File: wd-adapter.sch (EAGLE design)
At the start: 34 parts, among them Q1 BS170, Q2 BS170, Q3 BS170, Q4 BS170, Q5 BS170, Q6 BS170, T1 BC337, X2 KUSBVX

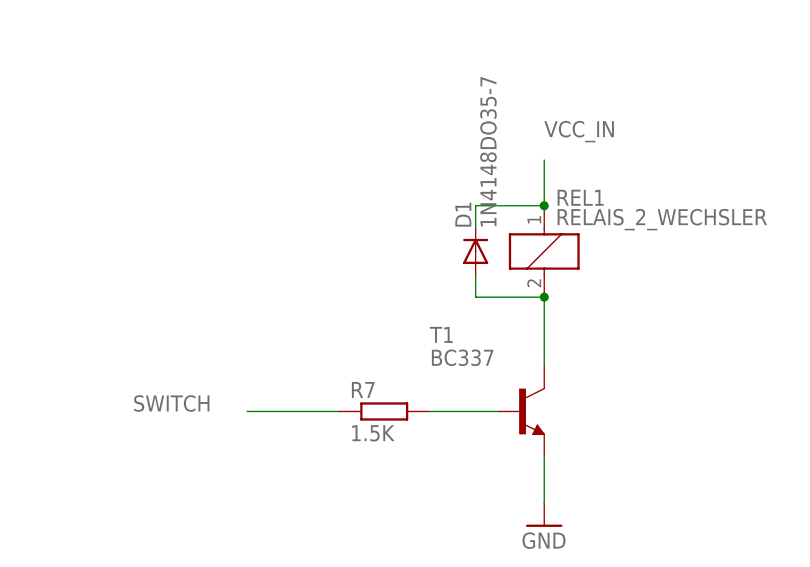
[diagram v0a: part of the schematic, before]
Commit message: Zustands-LED eingebaut
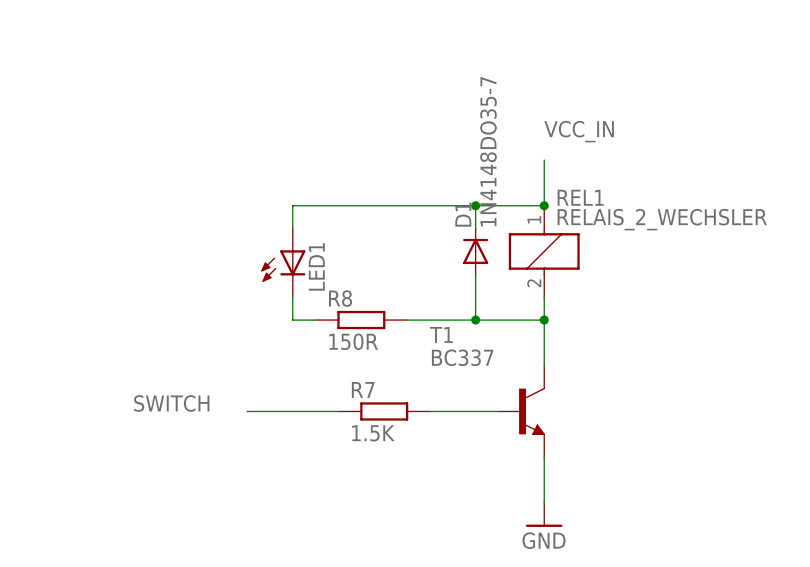
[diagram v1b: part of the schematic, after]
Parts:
- added LED1: (no value), led:LED3MM
- added R8: 150R, resistor:R-EU_0207/2V
- R7: device resistor:R-EU_0207/10 -> resistor:R-EU_0207/7
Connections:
- removed net N$19: D1.A, REL1SP.2, T1.C
- new net N$10: LED1.C, R8.1
- new net N$18: D1.A, R8.2, REL1SP.2, T1.C
- net VCC_IN: now also LED1.A
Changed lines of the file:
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@@
 <part name="D1" library="diode" deviceset="1N4148" device="DO35-7"/>
 <part name="GND6" library="supply1" deviceset="GND" device=""/>
-<part name="R7" library="resistor" deviceset="R-EU_" device="0207/10" value="1.5K"/>
+<part name="R7" library="resistor" deviceset="R-EU_" device="0207/7" value="1.5K"/>
 <part name="SUPPLY9" library="supply2" deviceset="VEE" device=""/>
 <part name="SUPPLY5" library="supply2" deviceset="VEE" device=""/>
 <part name="SUPPLY7" library="supply2" deviceset="VCC" device=""/>
+<part name="LED1" library="led" deviceset="LED" device="3MM"/>
+<part name="R8" library="resistor" deviceset="R-EU_" device="0207/2V" value="150R"/>
 </parts>
 <sheets>
@@
 <instance part="SUPPLY5" gate="G$1" x="162.56" y="-58.42"/>
 <instance part="SUPPLY7" gate="G$1" x="142.24" y="-58.42"/>
+<instance part="LED1" gate="G$1" x="81.28" y="-73.66"/>
+<instance part="R8" gate="G$1" x="88.9" y="-81.28"/>
 </instances>
 <busses>
@@
 <junction x="109.22" y="-68.58"/>
 <label x="109.22" y="-60.96" size="1.778" layer="95"/>
-</segment>
-</net>
-<net name="N$19" class="0">
-<segment>
-<pinref part="D1" gate="G$1" pin="A"/>
-<pinref part="REL1" gate="SP" pin="2"/>
-<wire x1="101.6" y1="-76.2" x2="101.6" y2="-78.74" width="0.1524" layer="91"/>
-<wire x1="101.6" y1="-78.74" x2="109.22" y2="-78.74" width="0.1524" layer="91"/>
-<pinref part="T1" gate="G$1" pin="C"/>
-<wire x1="109.22" y1="-78.74" x2="109.22" y2="-86.36" width="0.1524" layer="91"/>
-<junction x="109.22" y="-78.74"/>
+<wire x1="101.6" y1="-68.58" x2="81.28" y2="-68.58" width="0.1524" layer="91"/>
+<junction x="101.6" y="-68.58"/>
+<pinref part="LED1" gate="G$1" pin="A"/>
+<wire x1="81.28" y1="-68.58" x2="81.28" y2="-71.12" width="0.1524" layer="91"/>
 </segment>
 </net>
@@
 </segment>
 </net>
+<net name="N$10" class="0">
+<segment>
+<pinref part="LED1" gate="G$1" pin="C"/>
+<wire x1="81.28" y1="-78.74" x2="81.28" y2="-81.28" width="0.1524" layer="91"/>
+<pinref part="R8" gate="G$1" pin="1"/>
+<wire x1="81.28" y1="-81.28" x2="83.82" y2="-81.28" width="0.1524" layer="91"/>
+</segment>
+</net>
+<net name="N$18" class="0">
+<segment>
+<pinref part="D1" gate="G$1" pin="A"/>
+<wire x1="101.6" y1="-76.2" x2="101.6" y2="-81.28" width="0.1524" layer="91"/>
+<pinref part="R8" gate="G$1" pin="2"/>
+<wire x1="93.98" y1="-81.28" x2="101.6" y2="-81.28" width="0.1524" layer="91"/>
+<pinref part="REL1" gate="SP" pin="2"/>
+<pinref part="T1" gate="G$1" pin="C"/>
+<wire x1="109.22" y1="-78.74" x2="109.22" y2="-81.28" width="0.1524" layer="91"/>
+<wire x1="109.22" y1="-81.28" x2="109.22" y2="-86.36" width="0.1524" layer="91"/>
+<wire x1="101.6" y1="-81.28" x2="109.22" y2="-81.28" width="0.1524" layer="91"/>
+<junction x="101.6" y="-81.28"/>
+<junction x="109.22" y="-81.28"/>
+</segment>
+</net>
